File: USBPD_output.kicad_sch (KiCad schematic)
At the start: 32 parts, among them J2 Bus_RJ45_7499111121A, J3 USB-C_GCT_USB4105-GF-A, U10 TPD4E05U06QDQARQ1, U3 INA230AIRGTR, U6 TPS65987DDHRSHR

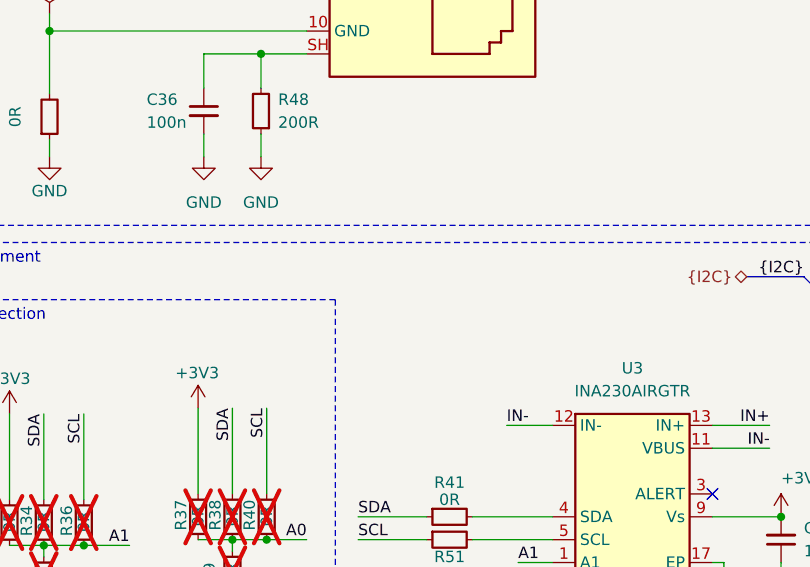
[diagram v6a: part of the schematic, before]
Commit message: [#63274] Add testpoints, improve silcscreen
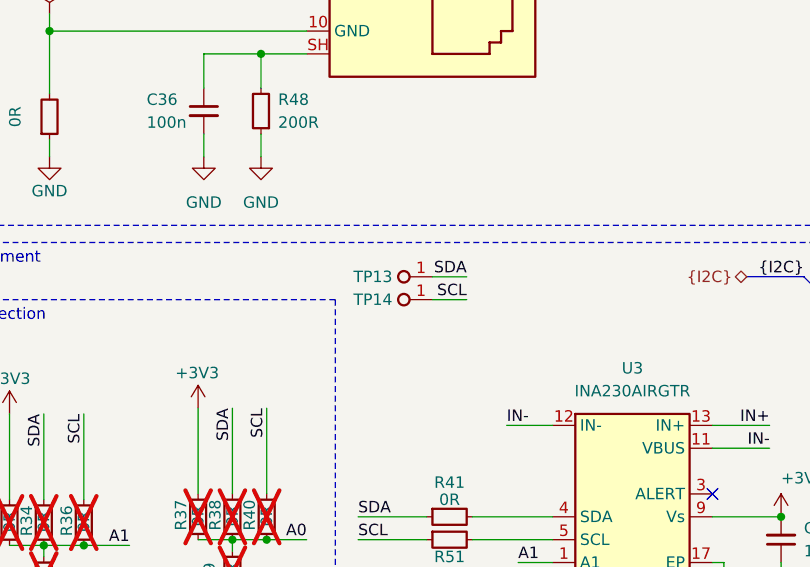
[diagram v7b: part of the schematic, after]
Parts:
- added TP13, TP14: TP_0.75mm_SMD, antmicro-footprints:TP_SMD_0.75mm, symbol antmicroTestPoints:TP_0.75mm_SMD
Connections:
- net SCL: now also TP14.1
- net SDA: now also TP13.1
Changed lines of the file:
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@@
+    (stroke (width 0) (type default))
+  )
+  (wire (pts (xy 140.335 195.58) (xy 144.145 195.58))
     (stroke (width 0) (type default))
   )
@@
   )
   (wire (pts (xy 232.41 182.88) (xy 241.3 182.88))
+    (stroke (width 0) (type default))
+  )
+  (wire (pts (xy 140.335 198.12) (xy 144.145 198.12))
     (stroke (width 0) (type default))
   )
@@
     (effects (font (size 1.27 1.27)) (justify left bottom))
   )
+  (label "SDA" (at 144.145 195.58 180) (fields_autoplaced)
+    (effects (font (size 1.27 1.27)) (justify right bottom))
+  )
   (label "MDI1_P" (at 187.96 137.16 180) (fields_autoplaced)
     (effects (font (size 1.27 1.27)) (justify right bottom))
@@
   )
   (label "MDI0_N" (at 187.96 134.62 180) (fields_autoplaced)
+    (effects (font (size 1.27 1.27)) (justify right bottom))
+  )
+  (label "SCL" (at 144.145 198.12 180) (fields_autoplaced)
     (effects (font (size 1.27 1.27)) (justify right bottom))
   )
@@
     )
   )
+  (symbol (lib_id "antmicroTestPoints:TP_0.75mm_SMD") (at 140.335 195.58 0) (mirror y) (unit 1)
+    (in_bom no) (on_board yes) (dnp no)
+    (property "Reference" "TP13" (at 135.89 195.58 0)
+      (effects (font (size 1.27 1.27) (thickness 0.15)) (justify left))
+    )
+    (property "Value" "TP_0.75mm_SMD" (at 130.175 199.39 0)
+      (effects (font (size 1.27 1.27) (thickness 0.15)) (justify left bottom) hide)
+    )
+    (property "Footprint" "antmicro-footprints:TP_SMD_0.75mm" (at 130.175 201.93 0)
+      (effects (font (size 1.27 1.27) (thickness 0.15)) (justify left bottom) hide)
+    )
+    (property "Datasheet" "" (at 122.555 208.28 0)
+      (effects (font (size 1.27 1.27) (thickness 0.15)) (justify left bottom) hide)
+    )
+    (property "MPN" "" (at 129.54 207.01 0)
+      (effects (font (size 1.27 1.27) (thickness 0.15)) (justify left bottom) hide)
+    )
+    (property "Manufacturer" "" (at 129.54 201.93 0)
+      (effects (font (size 1.27 1.27) (thickness 0.15)) (justify left bottom) hide)
+    )
+    (property "Author" "Antmicro" (at 130.175 204.47 0)
+      (effects (font (size 1.27 1.27) (thickness 0.15)) (justify left bottom) hide)
+    )
+    (property "License" "Apache-2.0" (at 130.175 207.01 0)
+      (effects (font (size 1.27 1.27) (thickness 0.15)) (justify left bottom) hide)
+    )
+    (pin "1")
+    (instances
+      (project "antmicro-poe-to-usbc-pd-adapter"
+        (path "/cf0d4429-3f03-449f-96a7-26d69371a46d/71fd6a9f-e91f-4e27-909c-676c68ed5a18"
+          (reference "TP13") (unit 1)
+        )
+      )
+    )
+  )
   (symbol (lib_id "antmicroResistors0402:R_0R_0402") (at 97.155 231.775 90) (unit 1)
     (in_bom no) (on_board yes) (dnp yes)
@@
         )
       )
+    )
+  )
+  (symbol (lib_id "antmicroTestPoints:TP_0.75mm_SMD") (at 140.335 198.12 0) (mirror y) (unit 1)
+    (in_bom no) (on_board yes) (dnp no)
+    (property "Reference" "TP14" (at 135.89 198.12 0)
+      (effects (font (size 1.27 1.27) (thickness 0.15)) (justify left))
+    )
+    (property "Value" "TP_0.75mm_SMD" (at 130.175 201.93 0)
+      (effects (font (size 1.27 1.27) (thickness 0.15)) (justify left bottom) hide)
+    )
+    (property "Footprint" "antmicro-footprints:TP_SMD_0.75mm" (at 130.175 204.47 0)
+      (effects (font (size 1.27 1.27) (thickness 0.15)) (justify left bottom) hide)
+    )
+    (property "Datasheet" "" (at 122.555 210.82 0)
+      (effects (font (size 1.27 1.27) (thickness 0.15)) (justify left bottom) hide)
+    )
+    (property "MPN" "" (at 129.54 209.55 0)
+      (effects (font (size 1.27 1.27) (thickness 0.15)) (justify left bottom) hide)
+    )
+    (property "Manufacturer" "" (at 129.54 204.47 0)
+      (effects (font (size 1.27 1.27) (thickness 0.15)) (justify left bottom) hide)
+    )
+    (property "Author" "Antmicro" (at 130.175 207.01 0)
+      (effects (font (size 1.27 1.27) (thickness 0.15)) (justify left bottom) hide)
+    )
+    (property "License" "Apache-2.0" (at 130.175 209.55 0)
+      (effects (font (size 1.27 1.27) (thickness 0.15)) (justify left bottom) hide)
+    )
+    (pin "1")
+    (instances
+      (project "antmicro-poe-to-usbc-pd-adapter"
+        (path "/cf0d4429-3f03-449f-96a7-26d69371a46d/71fd6a9f-e91f-4e27-909c-676c68ed5a18"
+          (reference "TP14") (unit 1)
+        )
+      )

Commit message: [#64013] Prepare production fixes
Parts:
- added R69: R_10k_0402, antmicro-footprints:R_0402_1005Metric, symbol antmicroResistors0402:R_10k_0402
- C16: now fitted; now in the parts list
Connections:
- net +3V3: now also R69.2
- net at U3.3 (ALERT): now also R69.1
- no-connect marks 9 -> 8
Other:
- company: Antmicro ltd. -> Antmicro Ltd.
- moved on the sheet: C15, C36, C38, C41, C46, C48, FB1, J2, J3, R33, R34, R35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
